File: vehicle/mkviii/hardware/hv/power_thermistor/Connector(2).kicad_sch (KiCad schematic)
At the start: 1 part, among them J3 T2M-110-01-X-D-TH-WT

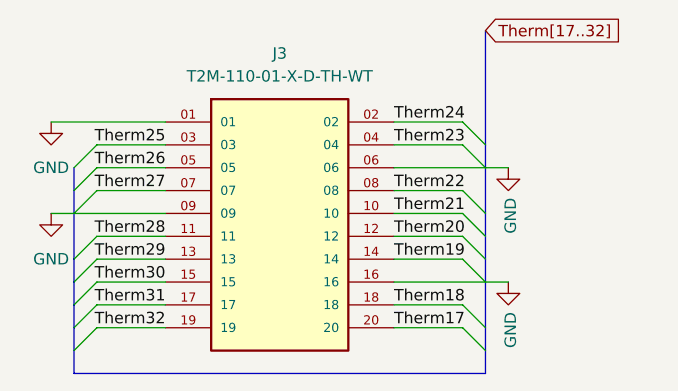
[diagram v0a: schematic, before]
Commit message: Power Therm overhall, have not been reviewed yet
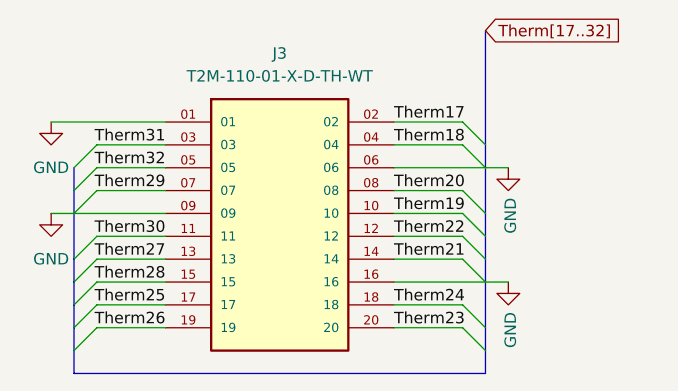
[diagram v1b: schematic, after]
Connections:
- net Therm17: now also J3.02; no longer J3.20
- net Therm18: now also J3.04; no longer J3.18
- net Therm19: now also J3.10; no longer J3.14
- net Therm20: now also J3.08; no longer J3.12
- net Therm21: now also J3.14; no longer J3.10
- net Therm22: now also J3.12; no longer J3.08
- net Therm23: now also J3.20; no longer J3.04
- net Therm24: now also J3.18; no longer J3.02
- net Therm25: now also J3.17; no longer J3.03
- net Therm26: now also J3.19; no longer J3.05
- net Therm27: now also J3.13; no longer J3.07
- net Therm28: now also J3.15; no longer J3.11
- net Therm29: now also J3.07; no longer J3.13
- net Therm30: now also J3.11; no longer J3.15
- net Therm31: now also J3.03; no longer J3.17
- net Therm32: now also J3.05; no longer J3.19
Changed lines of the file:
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@@
 		)
 	)
-	(label "Therm29"
+	(label "Therm27"
 		(at 52.07 54.61 180)
 		(effects
@@
 		)
 	)
-	(label "Therm18"
+	(label "Therm24"
 		(at 77.47 59.69 0)
 		(effects
@@
 		)
 	)
-	(label "Therm32"
+	(label "Therm26"
 		(at 52.07 62.23 180)
 		(effects
@@
 		)
 	)
-	(label "Therm24"
+	(label "Therm17"
 		(at 77.47 39.37 0)
 		(effects
@@
 		)
 	)
-	(label "Therm17"
+	(label "Therm23"
 		(at 77.47 62.23 0)
 		(effects
@@
 		)
 	)
-	(label "Therm31"
+	(label "Therm25"
 		(at 52.07 59.69 180)
 		(effects
@@
 		)
 	)
-	(label "Therm26"
+	(label "Therm32"
 		(at 52.07 44.45 180)
 		(effects
@@
 		)
 	)
-	(label "Therm19"
+	(label "Therm21"
 		(at 77.47 54.61 0)
 		(effects
@@
 		)
 	)
-	(label "Therm21"
+	(label "Therm19"
 		(at 77.47 49.53 0)
 		(effects
@@
 		)
 	)
-	(label "Therm23"
+	(label "Therm18"
 		(at 77.47 41.91 0)
 		(effects
@@
 		)
 	)
-	(label "Therm28"
+	(label "Therm30"
 		(at 52.07 52.07 180)
 		(effects
@@
 		)
 	)
-	(label "Therm20"
+	(label "Therm22"
 		(at 77.47 52.07 0)
 		(effects
@@
 		)
 	)
-	(label "Therm27"
+	(label "Therm29"
 		(at 52.07 46.99 180)
 		(effects
@@
 		)
 	)
-	(label "Therm22"
+	(label "Therm20"
 		(at 77.47 46.99 0)
 		(effects
@@
 		)
 	)
-	(label "Therm25"
+	(label "Therm31"
 		(at 52.07 41.91 180)
 		(effects
@@
 		)
 	)
-	(label "Therm30"
+	(label "Therm28"
 		(at 52.07 57.15 180)
 		(effects

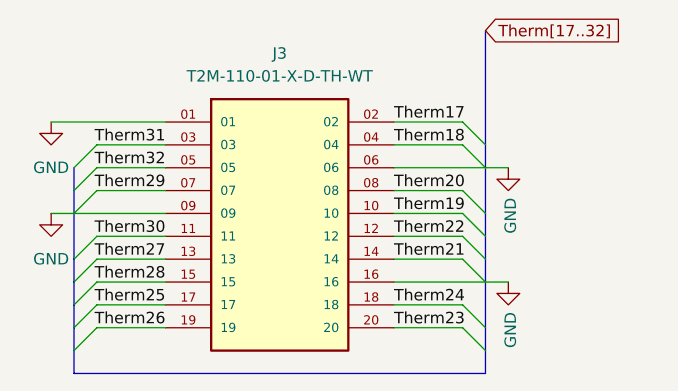
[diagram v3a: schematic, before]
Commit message: fixes for connector to BMS MOBO
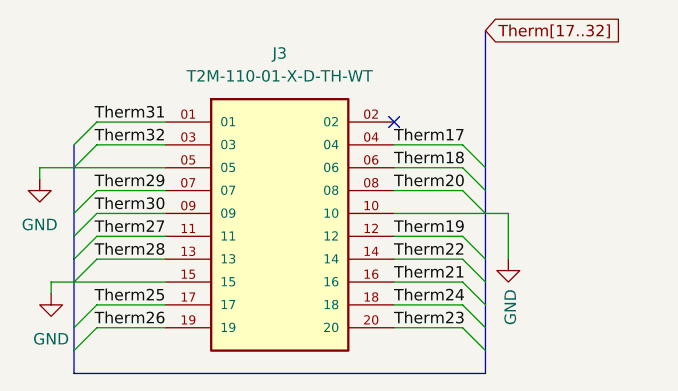
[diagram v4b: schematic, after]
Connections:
- net GND: now also J3.05, J3.10, J3.15; no longer J3.01, J3.06, J3.09, J3.16
- net Therm17: now also J3.04; no longer J3.02
- net Therm18: now also J3.06; no longer J3.04
- net Therm19: now also J3.12; no longer J3.10
- net Therm21: now also J3.16; no longer J3.14
- net Therm22: now also J3.14; no longer J3.12
- net Therm27: now also J3.11; no longer J3.13
- net Therm28: now also J3.13; no longer J3.15
- net Therm30: now also J3.09; no longer J3.11
- net Therm31: now also J3.01; no longer J3.03
- net Therm32: now also J3.03; no longer J3.05
- no-connect marks 0 -> 1
